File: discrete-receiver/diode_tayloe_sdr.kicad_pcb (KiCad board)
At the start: 4 copper layers, 110 x 110 mm, 268 parts, among them J2 Optional 5V DC Jack, J3 External Filter, J4 Debug Pins, J5 Display Connector, J6 SI-52003-F, T1 H1102NLT, T2 MABA-007159-000000, U1 SN74CBT3253DBQR, U10 MS5351M, U11 Ag9905LP, U13 LM66100DCK, U14 LM66100DCK, U15 LM66100DCK, U16 PSA4-5043_, U2 OPA1612AxD, U3 OPA1612AxD, U4 CJC5340, U5 ADE-1+, U6 RP2350A, U7 W25Q128, U9 LAN8720A, X1 YC24.576MUBCE2O, X2 X322512MSB4SI

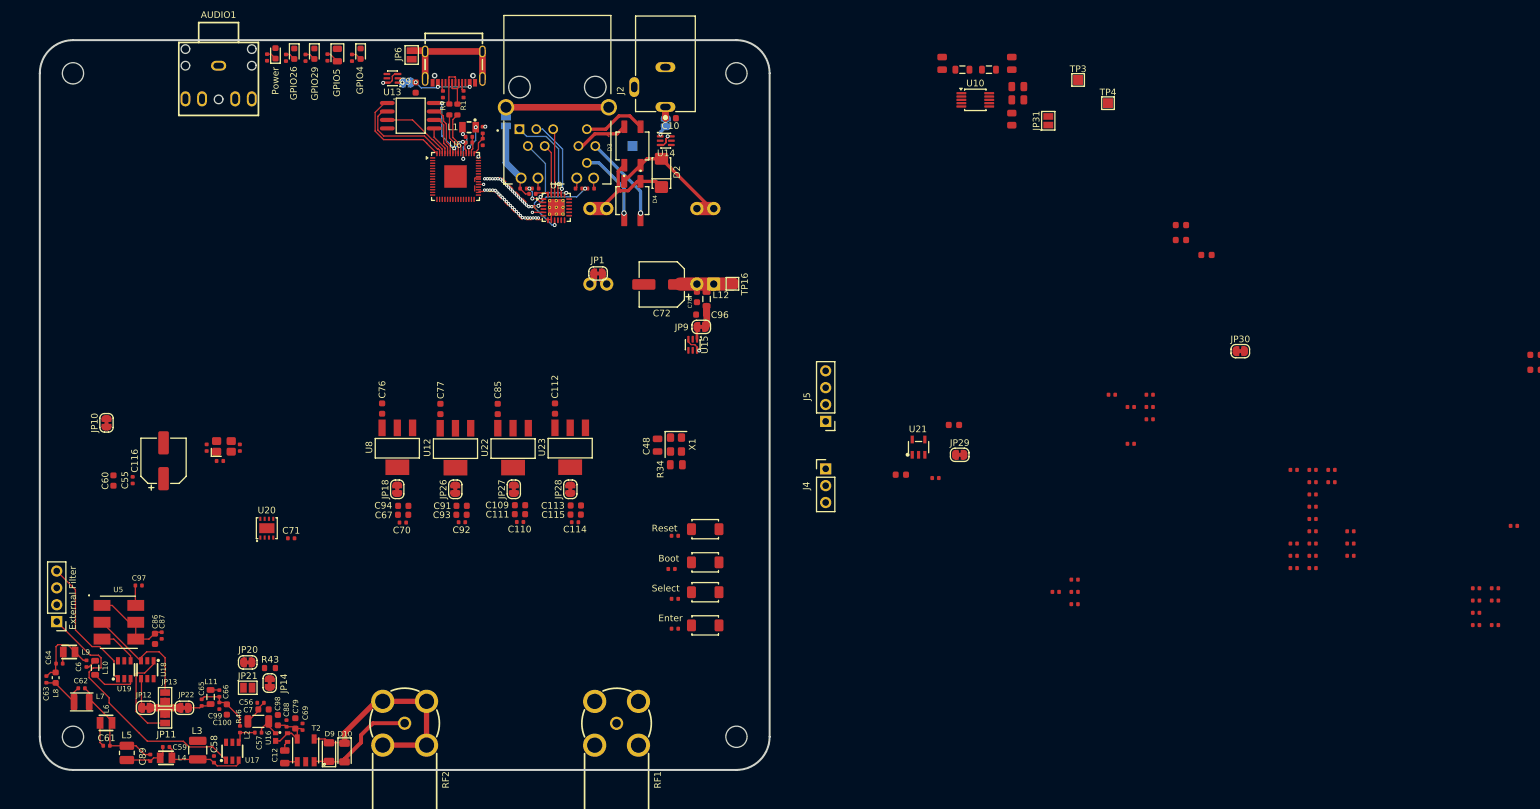
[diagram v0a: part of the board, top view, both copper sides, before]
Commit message: PCB progress
Working on RMII lines
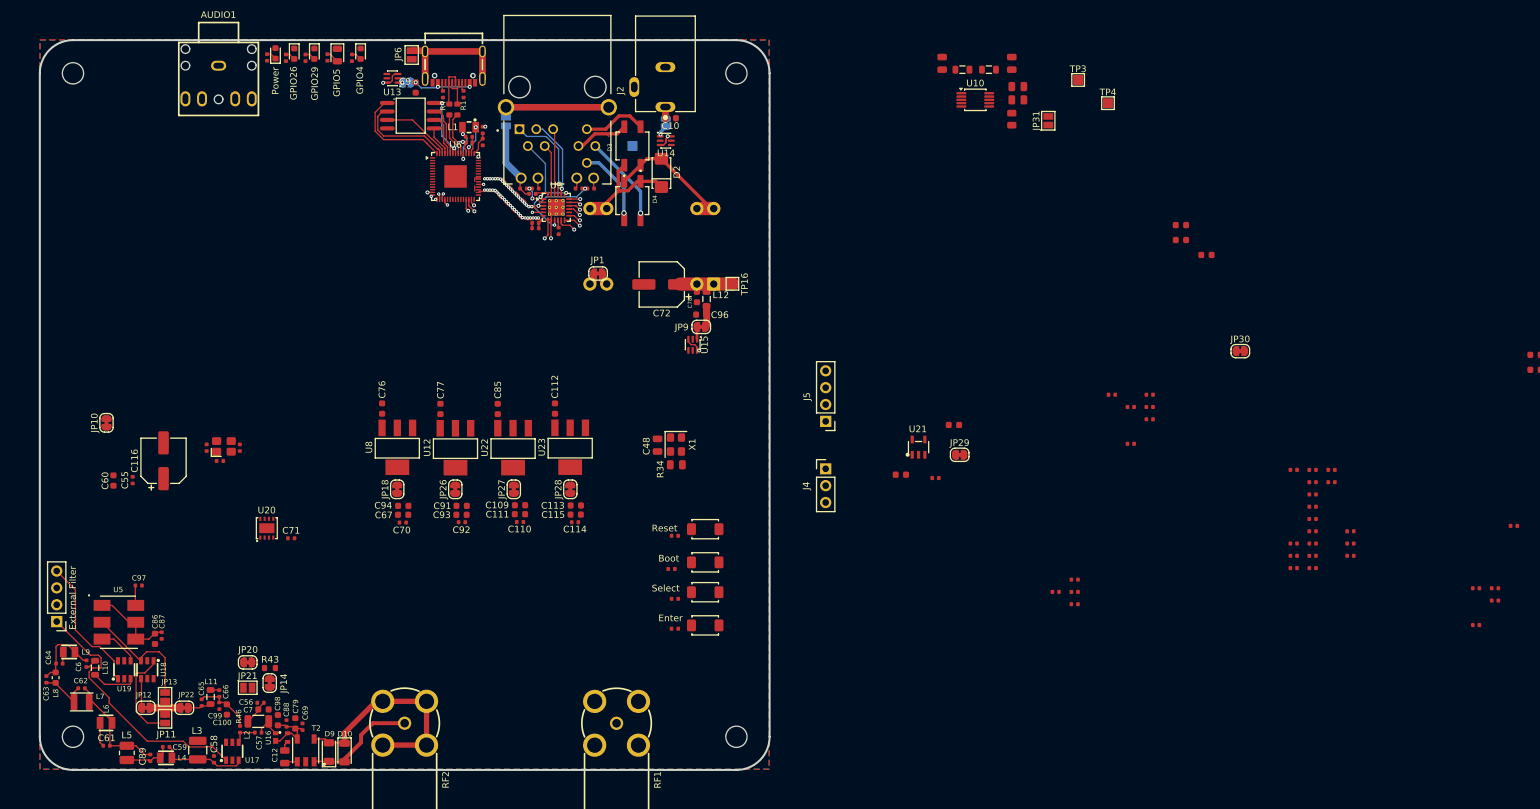
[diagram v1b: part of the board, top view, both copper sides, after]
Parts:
- moved C51 153.5 mm to (107.2, 59.0), turned to 180 degrees
- moved R25 153.1 mm to (110.7, 60.2), turned to -90 degrees
- moved C50 152.5 mm to (107.2, 59.9), turned to 180 degrees
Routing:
- net /Ethernet Interface/ETH_TX_EN: track 0.00 -> 31.0 mm, vias 0 -> 2
- net /Ethernet Interface/ETH_CRS_DV: track 0.00 -> 30.0 mm, vias 0 -> 2
- net /Ethernet Interface/ETH_TXD0: track 0.00 -> 29.1 mm, vias 0 -> 2
- net /Ethernet Interface/ETH_TXD1: track 0.00 -> 28.0 mm, vias 0 -> 2
- net /Ethernet Interface/ETH_RXD0: track 0.00 -> 24.3 mm, vias 0 -> 2
- net /Ethernet Interface/ETH_MDIO: track 0.00 -> 23.3 mm, vias 0 -> 2
- net /Ethernet Interface/ETH_MDC: track 0.00 -> 22.0 mm, vias 0 -> 2
- net /Ethernet Interface/nRST: track 0.00 -> 21.5 mm, vias 0 -> 2
- net /Ethernet Interface/ETH_RXD1: track 0.00 -> 21.1 mm, vias 0 -> 2
- net Net-(U9-VDDCR): track 0.00 -> 2.19 mm
- net Net-(U9-RXER/PHYAD0): track 0.00 -> 1.15 mm
- net GND: track 19.5 -> 20.3 mm
- added copper zone on B.Cu, net GND

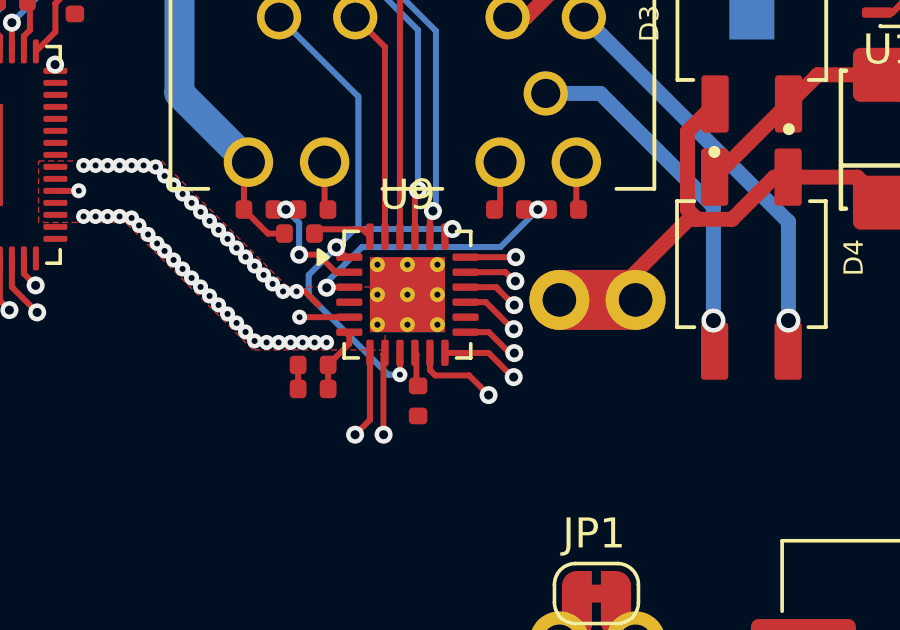
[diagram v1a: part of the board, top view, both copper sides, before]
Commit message: RMII lines routed
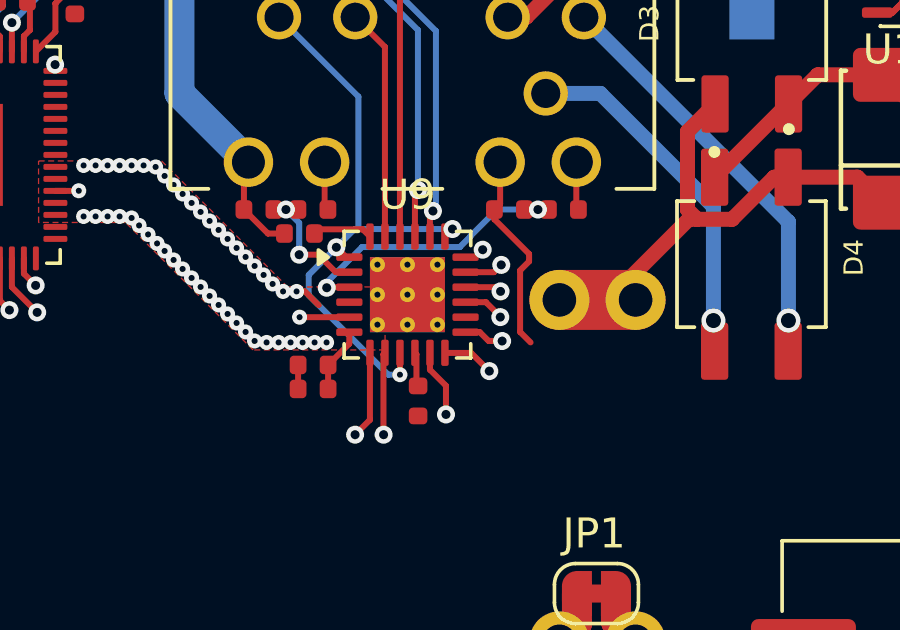
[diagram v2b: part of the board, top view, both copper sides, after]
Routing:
- net GND: track 20.3 -> 25.5 mm
- net /Ethernet Interface/ETH_CRS_DV: track 30.0 -> 27.1 mm
- net /Ethernet Interface/ETH_MDIO: track 23.3 -> 21.7 mm
- net /Ethernet Interface/ETH_TXD1: track 28.0 -> 26.8 mm
- net /Ethernet Interface/nRST: track 21.5 -> 20.5 mm
- net /Ethernet Interface/ETH_MDC: track 22.0 -> 21.1 mm

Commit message: Made Ag9905 DNP
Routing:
- net Net-(JP10-B): track 10.7 -> 53.3 mm
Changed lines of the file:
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@@
+	)
+	(segment
+		(start 139.7 70.465)
+		(end 131.895 78.27)
+		(width 0.5)
+		(layer "In2.Cu")
+		(net "Net-(JP10-B)")
+	)
+	(segment
+		(start 139.7 55.4)
+		(end 139.7 70.465)
+		(width 0.5)
+		(layer "In2.Cu")
+		(net "Net-(JP10-B)")
+	)
+	(segment
+		(start 127.138689 45.992123)
+		(end 130.292123 45.992123)
+		(width 0.5)
+		(layer "In2.Cu")
+		(net "Net-(JP10-B)")
+	)
+	(segment
+		(start 130.292123 45.992123)
+		(end 139.7 55.4)
+		(width 0.5)
+		(layer "In2.Cu")
+		(net "Net-(JP10-B)")
 	)
 	(segment

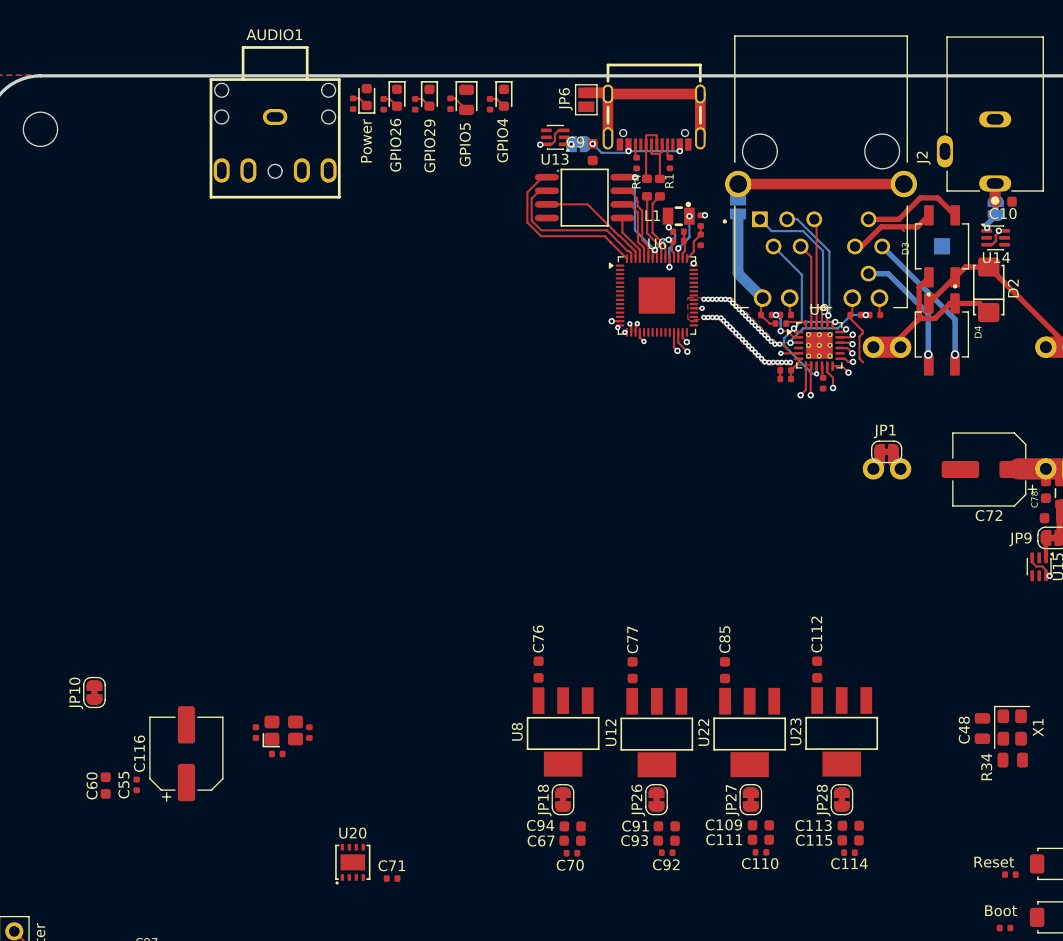
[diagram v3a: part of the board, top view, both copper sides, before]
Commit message: Progress on 3.3V regulators
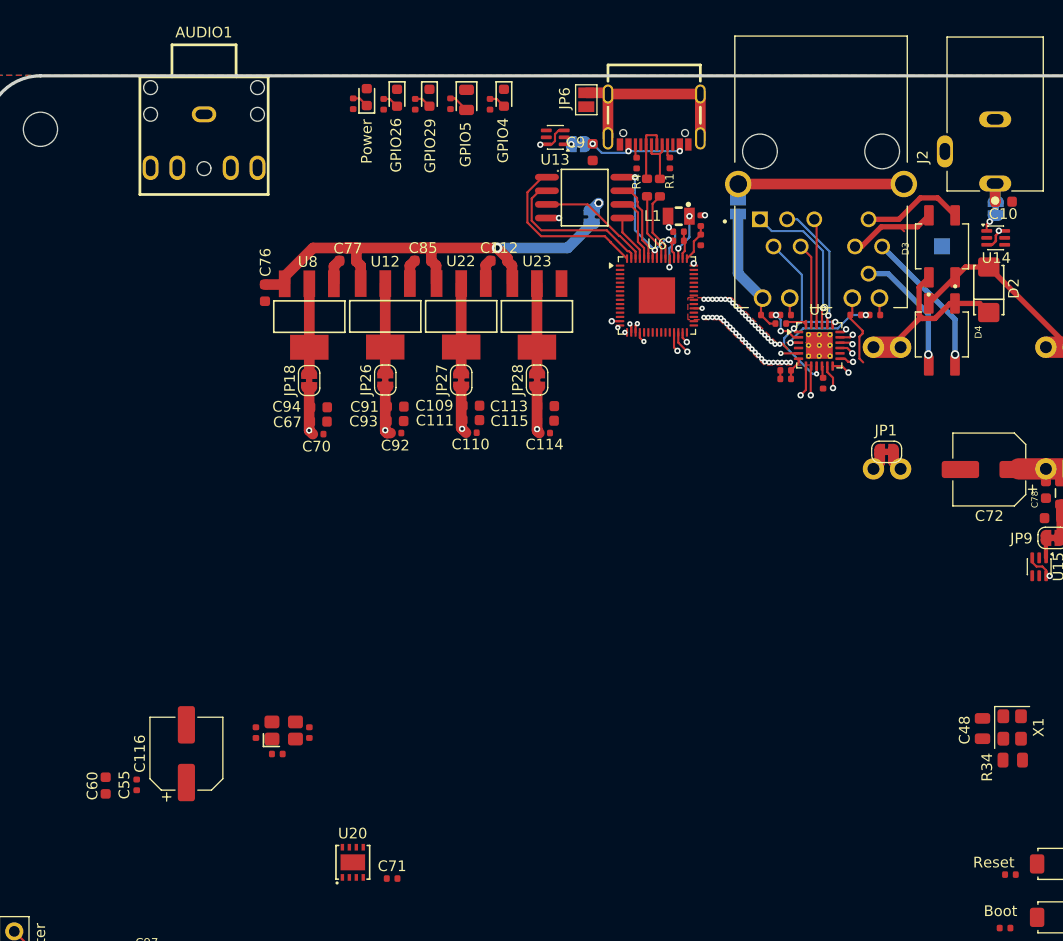
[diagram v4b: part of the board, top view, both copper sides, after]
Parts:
- JP10: moved to B.Cu
- moved JP10 64.3 mm to (89.0, 44.7)
- moved C114 48.5 mm to (84.7, 64.9)
- moved C115 48.5 mm to (84.8, 63.8)
- moved C113 48.5 mm to (84.8, 62.4)
- moved JP28 48.5 mm to (84.0, 60.0)
- moved C112 48.4 mm to (80.4, 48.8), turned to 0 degrees
- moved U23 48.3 mm to (83.9, 53.9)
- moved C110 47.7 mm to (77.8, 64.9)
- moved JP27 47.7 mm to (76.8, 60.0)
- moved C111 47.7 mm to (77.8, 63.7)
- moved C109 47.7 mm to (77.8, 62.4)
- moved C85 47.6 mm to (73.3, 48.8), turned to 0 degrees
- moved U22 47.5 mm to (76.8, 53.9)
- moved C93 46.7 mm to (70.7, 63.8)
- moved C91 46.7 mm to (70.7, 62.4)
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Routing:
- net +5V: track 0.00 -> 47.7 mm, vias 0 -> 1
- net Net-(JP10-B): track 53.3 -> 100.4 mm, vias 3 -> 4
- net Net-(JP18-B): track 0.00 -> 8.41 mm
- net Net-(JP28-B): track 0.00 -> 8.37 mm
- net Net-(JP27-B): track 0.00 -> 8.37 mm
- net Net-(JP26-B): track 0.00 -> 8.37 mm
- net GND: track 25.5 -> 33.6 mm, vias 47 -> 48
- net +3.3V_ADC: track 0.00 -> 4.72 mm, vias 0 -> 1
- net +3.3V: track 51.2 -> 55.7 mm, vias 8 -> 9
- net +3.3V_SI5351: track 0.00 -> 4.47 mm, vias 0 -> 1
- net +3.3V_CLK: track 0.00 -> 4.40 mm, vias 0 -> 1

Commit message: Progress on power regulation
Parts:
- JP29, JP30: moved to B.Cu
- moved JP30 160.5 mm to (54.8, 54.4)
- moved C90 155.2 mm to (53.6, 51.9), turned to 90 degrees
- moved C34 153.5 mm to (51.2, 53.4), turned to 90 degrees
- moved C32 152.2 mm to (52.5, 53.4), turned to 90 degrees
- moved R35 148.6 mm to (54.3, 58.5), turned to -90 degrees
- moved R27 148.6 mm to (54.3, 56.6), turned to -90 degrees
- moved C33 147.3 mm to (50.2, 53.4), turned to 90 degrees
- moved C95 146.2 mm to (53.5, 58.5), turned to 90 degrees
- moved R3 145.8 mm to (56.0, 54.9), turned to 180 degrees
- moved R10 145.1 mm to (57.9, 54.9)
- moved JP29 120.4 mm to (55.7, 59.8), turned to 90 degrees
- moved C75 119.6 mm to (54.2, 60.5), turned to 180 degrees
- moved C74 118.9 mm to (54.1, 61.5), turned to 180 degrees
- moved U21 114.1 mm to (56.5, 57.3)
- moved C73 111.3 mm to (57.1, 60.5)
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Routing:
- net Net-(JP29-B): track 0.00 -> 6.99 mm, vias 0 -> 1
- net +5V: track 47.7 -> 53.6 mm, vias 1 -> 3
- net Net-(U21-VIN+): track 0.00 -> 5.75 mm
- net Net-(JP30-B): track 0.00 -> 4.17 mm, vias 0 -> 1
- net +4.8V_A: track 0.00 -> 4.14 mm, vias 0 -> 1
- net +2.4V_A: track 37.4 -> 39.9 mm, vias 0 -> 1
- net Net-(U20-FB): track 0.00 -> 1.86 mm
- net Net-(U20-NR): track 0.00 -> 0.98 mm
- net GND: track 33.6 -> 34.4 mm, vias 48 -> 51
